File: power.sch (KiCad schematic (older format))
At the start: 38 parts, among them J2 USB_C_Receptacle_USB2.0, J3 TagConnect_TC2030_SWD, Q1 FS8205A, Q6 2N7002, Q7 AO3401A, SW8 SW_Push, U3 SY7088, U4 XC6206P332MR, U5 DW01+G, U6 TP4054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

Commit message: Add self-programming capability
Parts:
- removed C20, C21: 100nF, Capacitor_SMD:C_0402_1005Metric, symbol Device:C
- removed D5: PWR, Diode_SMD:D_0603_1608Metric, symbol Device:LED
- removed J3: TagConnect_TC2030_SWD, Connector:Tag-Connect_TC2030-IDC-NL_2x03_P1.27mm_Vertical, symbol Connector_TagConnect:TagConnect_TC2030_SWD
- removed R22: 8.2kR, Resistor_SMD:R_0402_1005Metric, symbol Device:R
- removed SW8: SW_Push, Button_Carbon:Button_Carbon_5mm, symbol Switch:SW_Push
- removed U8: STM32L011D3Px, Package_SO:TSSOP-14_4.4x5mm_P0.65mm, symbol MCU_ST_STM32L0:STM32L011D3Px
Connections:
- net labels removed: ~STMRST
- wire segments 156 -> 126
- no-connect marks 9 -> 3
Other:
- moved on the sheet: C11, C12, C13, C14, C15, C16, C17, C18, C19, D4, J2, L1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

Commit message: Add charge state/current sensing and VBUS wakeup source
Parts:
- added C?: 100nF, Capacitor_SMD:C_0402_1005Metric, symbol Device:C
- added F1, F2: Fuse, Fuse:Fuse_1206_3216Metric, symbol Device:Fuse
- added R? (x2): 8.2kR, Resistor_SMD:R_0402_1005Metric, symbol Device:R
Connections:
- net labels added: Ichg, LEDchg
- wire segments 126 -> 141
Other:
- moved on the sheet: TP1
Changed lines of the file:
@@
 L power:VBUS #PWR?
 U 1 1 6053CC12
-P 1700 3300
+P 1700 2950
 AR Path="/6053CC12" Ref="#PWR?"  Part="1"
 AR Path="/6051E9DC/6053CC12" Ref="#PWR023"  Part="1"
-F 0 "#PWR023" H 1700 3150 50  0001 C CNN
-F 1 "VBUS" H 1715 3473 50  0000 C CNN
-F 2 "" H 1700 3300 50  0001 C CNN
-F 3 "" H 1700 3300 50  0001 C CNN
-	1    1700 3300
+F 0 "#PWR023" H 1700 2800 50  0001 C CNN
+F 1 "VBUS" H 1715 3123 50  0000 C CNN
+F 2 "" H 1700 2950 50  0001 C CNN
+F 3 "" H 1700 2950 50  0001 C CNN
+	1    1700 2950
 	1    0    0    -1
 $EndComp
@@
 L Connector:TestPoint TP?
 U 1 1 6057E186
-P 4250 3550
+P 4250 3200
 AR Path="/6057E186" Ref="TP?"  Part="1"
 AR Path="/6051E9DC/6057E186" Ref="TP1"  Part="1"
-F 0 "TP1" H 4308 3668 50  0000 L CNN
-F 1 "BAT+" H 4308 3577 50  0000 L CNN
-F 2 "TestPoint:TestPoint_Pad_4.0x4.0mm" H 4450 3550 50  0001 C CNN
-F 3 "~" H 4450 3550 50  0001 C CNN
-	1    4250 3550
+F 0 "TP1" H 4308 3318 50  0000 L CNN
+F 1 "BAT+" H 4308 3227 50  0000 L CNN
+F 2 "TestPoint:TestPoint_Pad_4.0x4.0mm" H 4450 3200 50  0001 C CNN
+F 3 "~" H 4450 3200 50  0001 C CNN
+	1    4250 3200
 	1    0    0    -1
 $EndComp
@@
 	3700 3900 3650 3900
 Wire Wire Line
-	2700 3350 2700 3300
-Wire Wire Line
-	2700 4000 2700 4250
+	2700 4000 2700 4050
 $Comp
 L Device:LED D?
@@
 L power:VBUS #PWR?
 U 1 1 6057E1D9
-P 2700 3300
+P 2700 3250
 AR Path="/6057E1D9" Ref="#PWR?"  Part="1"
 AR Path="/6051E9DC/6057E1D9" Ref="#PWR037"  Part="1"
-F 0 "#PWR037" H 2700 3150 50  0001 C CNN
-F 1 "VBUS" H 2715 3473 50  0000 C CNN
-F 2 "" H 2700 3300 50  0001 C CNN
-F 3 "" H 2700 3300 50  0001 C CNN
-	1    2700 3300
+F 0 "#PWR037" H 2700 3100 50  0001 C CNN
+F 1 "VBUS" H 2715 3423 50  0000 C CNN
+F 2 "" H 2700 3250 50  0001 C CNN
+F 3 "" H 2700 3250 50  0001 C CNN
+	1    2700 3250
 	1    0    0    -1
 $EndComp
@@
 Text HLabel 9150 4850 0    50   Input ~ 0
 PWR_EN
+$Comp
+L Device:Fuse F1
+U 1 1 60F311E6
+P 1700 3150
+F 0 "F1" H 1760 3196 50  0000 L CNN
+F 1 "Fuse" H 1760 3105 50  0000 L CNN
+F 2 "Fuse:Fuse_1206_3216Metric" V 1630 3150 50  0001 C CNN
+F 3 "https://datasheet.lcsc.com/szlcsc/Shenzhen-lanson-Elec-12H1200C_C182310.pdf" H 1700 3150 50  0001 C CNN
+F 4 "C182310" H 1700 3150 50  0001 C CNN "LCSC"
+	1    1700 3150
+	1    0    0    -1
+$EndComp
+Wire Wire Line
+	1700 2950 1700 3000
+$Comp
+L Device:Fuse F2
+U 1 1 60F38C32
+P 4250 3400
+F 0 "F2" H 4310 3446 50  0000 L CNN
+F 1 "Fuse" H 4310 3355 50  0000 L CNN
+F 2 "Fuse:Fuse_1206_3216Metric" V 4180 3400 50  0001 C CNN
+F 3 "https://datasheet.lcsc.com/szlcsc/Shenzhen-lanson-Elec-12H1200C_C182310.pdf" H 4250 3400 50  0001 C CNN
+F 4 "C182310" H 4250 3400 50  0001 C CNN "LCSC"
+	1    4250 3400
+	-1   0    0    1
+$EndComp
+Wire Wire Line
+	4250 3250 4250 3200
+$Comp
+L Device:R R?
+U 1 1 60F9B087
+P 2500 4350
+AR Path="/60F9B087" Ref="R?"  Part="1"
+AR Path="/6051E9DC/60F9B087" Ref="R?"  Part="1"
+F 0 "R?" V 2293 4350 50  0000 C CNN
+F 1 "8.2kR" V 2384 4350 50  0000 C CNN
+F 2 "Resistor_SMD:R_0402_1005Metric" V 2430 4350 50  0001 C CNN
+F 3 "~" H 2500 4350 50  0001 C CNN
+F 4 "C25924" V 2500 4350 50  0001 C CNN "LCSC"
+	1    2500 4350
+	0    1    1    0
+$EndComp
+$Comp
+L Device:C C?
+U 1 1 60FA0E56
+P 2300 4550
+AR Path="/60FA0E56" Ref="C?"  Part="1"
+AR Path="/6051E9DC/60FA0E56" Ref="C?"  Part="1"
+F 0 "C?" V 2552 4550 50  0000 C CNN
+F 1 "100nF" V 2461 4550 50  0000 C CNN
+F 2 "Capacitor_SMD:C_0402_1005Metric" H 2338 4400 50  0001 C CNN
+F 3 "~" H 2300 4550 50  0001 C CNN
+F 4 "C1525" H 2300 4550 50  0001 C CNN "LCSC"
+	1    2300 4550
+	-1   0    0    1
+$EndComp
+Connection ~ 2700 4750
+Wire Wire Line
+	2650 4350 2700 4350
+Connection ~ 2700 4350
+Wire Wire Line
+	2300 4750 2300 4700
+Wire Wire Line
+	2300 4750 2700 4750
+Wire Wire Line
+	2350 4350 2300 4350
+Wire Wire Line
+	2300 4350 2300 4400
+Wire Wire Line
+	2250 4350 2300 4350
+Connection ~ 2300 4350
+Text HLabel 2250 4350 0    50   Output ~ 0
+Ichg
+$Comp
+L Device:R R?
+U 1 1 60FBF848
+P 2900 3500
+AR Path="/60FBF848" Ref="R?"  Part="1"
+AR Path="/6051E9DC/60FBF848" Ref="R?"  Part="1"
+F 0 "R?" V 2693 3500 50  0000 C CNN
+F 1 "8.2kR" V 2784 3500 50  0000 C CNN
+F 2 "Resistor_SMD:R_0402_1005Metric" V 2830 3500 50  0001 C CNN
+F 3 "~" H 2900 3500 50  0001 C CNN
+F 4 "C25924" V 2900 3500 50  0001 C CNN "LCSC"
+	1    2900 3500
+	-1   0    0    1
+$EndComp
+Wire Wire Line
+	2700 3250 2700 3300
+Wire Wire Line
+	2700 3300 2900 3300
+Wire Wire Line
+	2900 3300 2900 3350
+Connection ~ 2700 3300
+Wire Wire Line
+	2700 3300 2700 3350
+Wire Wire Line
+	2900 3650 2900 4050
+Wire Wire Line
+	2900 4050 2700 4050
+Connection ~ 2700 4050
+Wire Wire Line
+	2700 4050 2700 4250
+Text HLabel 2650 4050 0    50   Output ~ 0
+LEDchg
+Wire Wire Line
+	2650 4050 2700 4050
 $EndSCHEMATC

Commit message: Implement fuel gauging
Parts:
- added C27, C29: 100nF, Capacitor_SMD:C_0402_1005Metric, symbol Device:C
- added C28: 1uF, Capacitor_SMD:C_0402_1005Metric, symbol Device:C
- added R29: 1MR, Resistor_SMD:R_0402_1005Metric, symbol Device:R
- added R30, R31: 100R, Resistor_SMD:R_0402_1005Metric, symbol Device:R
- added R32: 25mR, Resistor_SMD:R_2512_6332Metric, symbol Device:R
- added TH1: 10kR 3380K, Resistor_SMD:R_0402_1005Metric, symbol Device:Thermistor_NTC
- added U9: BQ34Z100, Package_SO:TSSOP-14_4.4x5mm_P0.65mm, symbol Fuel_Gauge_TI:BQ34Z100
- gave numbers to parts that had none: 3
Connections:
- net labels added: GAUGE_EN, GNDREF, SCL, SDA, SHUNT+, SHUNT-
- wire segments 141 -> 183
- no-connect marks 3 -> 7

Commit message: Finish layout
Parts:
- removed U6: TP4054, Package_TO_SOT_SMD:TSOT-23-5, symbol Battery_Management:LTC4054ES5-4.2
- added C30: 100nF, Capacitor_SMD:C_0402_1005Metric, symbol Device:C
- added C31: 47uF, Capacitor_SMD:C_1206_3216Metric, symbol Device:C
- added Q8: 2N7002, Package_TO_SOT_SMD:SOT-23, symbol Transistor_FET:2N7002
- added R35: 1MR, Resistor_SMD:R_0402_1005Metric, symbol Device:R
- added R36: 8.2kR, Resistor_SMD:R_0402_1005Metric, symbol Device:R
- added U6: TP4056, Package_SO:HSOP-8-1EP_3.9x4.9mm_P1.27mm_EP2.41x3.1mm, symbol Battery_Management_Generic:TP4056
- C19: value 1uF -> 10uF; footprint Capacitor_SMD:C_0402_1005Metric -> Capacitor_SMD:C_0603_1608Metric; LCSC C52923 -> C19702
- C26: value 100nF -> 10uF; footprint Capacitor_SMD:C_0402_1005Metric -> Capacitor_SMD:C_0603_1608Metric; LCSC C1525 -> C19702
- R26: value 8.2kR -> 2.2kR; LCSC C25924 -> C25879
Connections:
- net labels added: ~PWR_EN
- wire segments 183 -> 205
- no-connect marks 7 -> 8
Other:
- note added: "Ichg=500mA/1A"
- note removed: "Ichg=450mA"
- moved on the sheet: C18, D4, F2, Q1, R12, R13, R14, R27, R32, TP1, TP2, U5

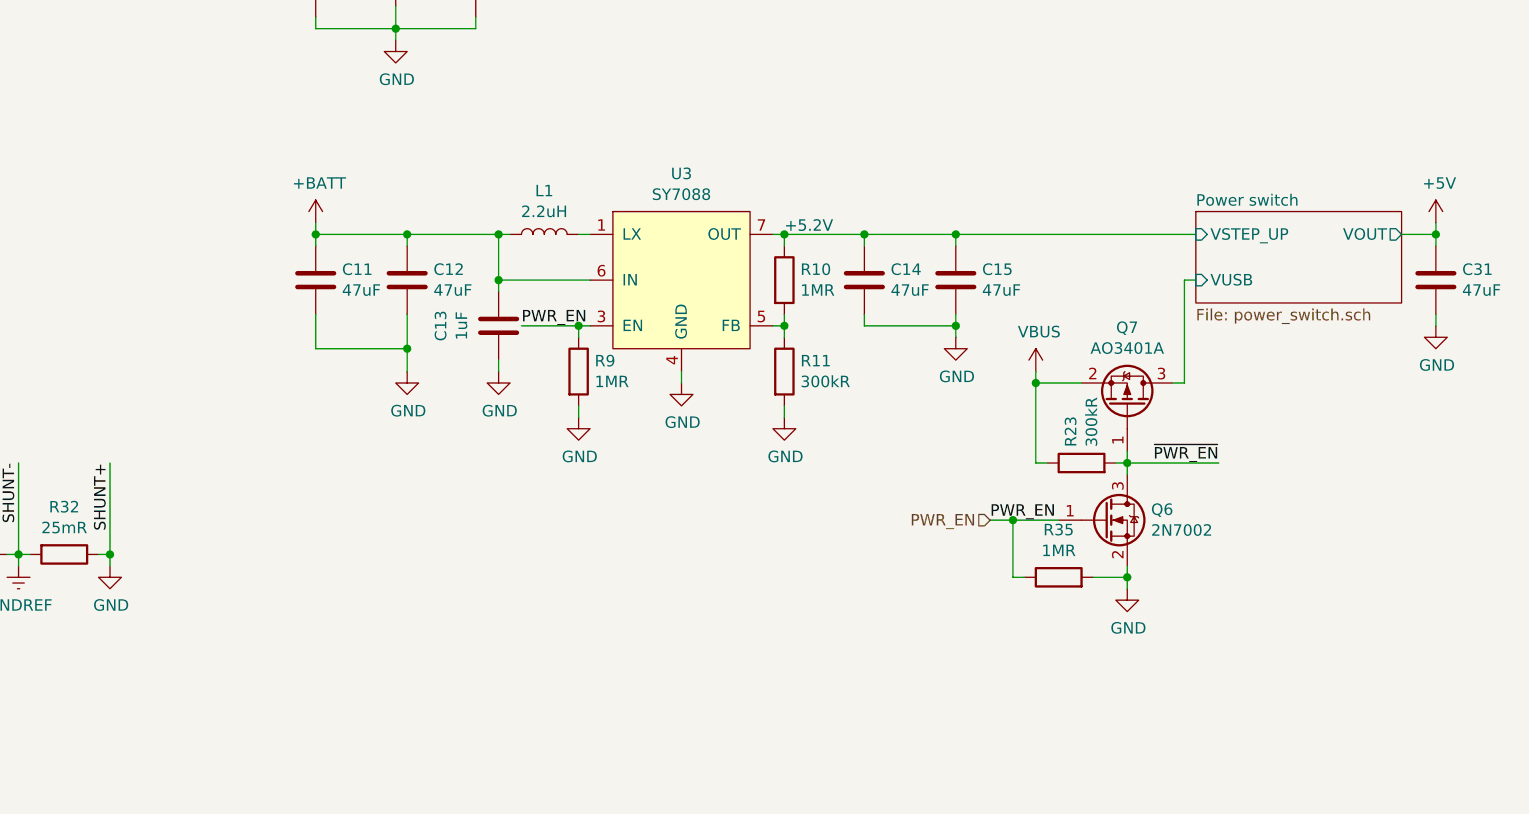
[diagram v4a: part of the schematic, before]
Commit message: Add additional mounting holes
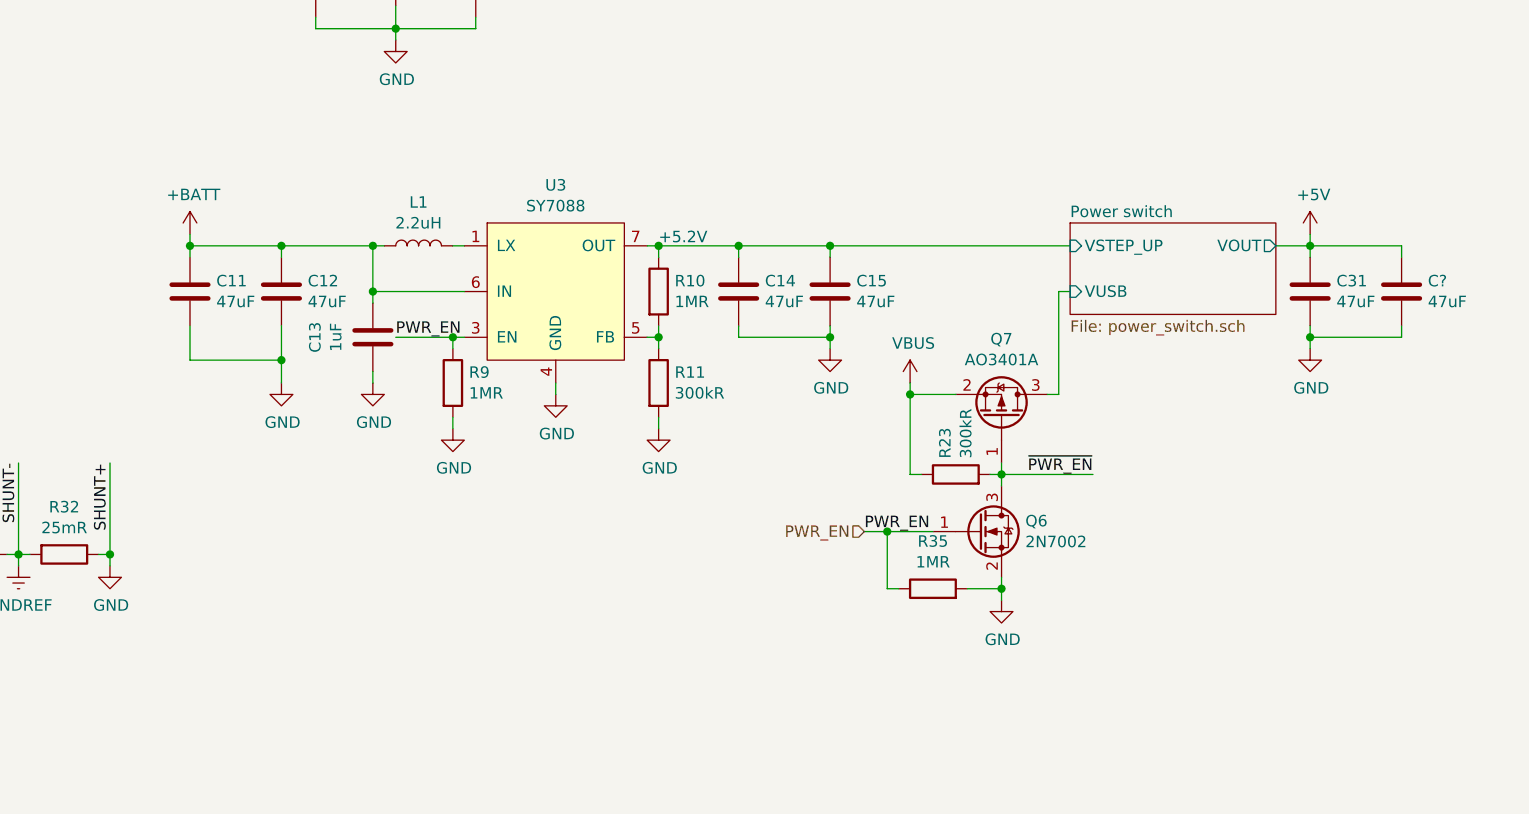
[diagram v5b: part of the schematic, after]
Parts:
- added C?: 47uF, Capacitor_SMD:C_1206_3216Metric, symbol Device:C
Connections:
- net +5V: now also C?.2
- net GND: now also C?.1
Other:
- moved on the sheet: C11, C12, C13, C14, C15, C31, L1, Q6, Q7, R10, R11, R23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

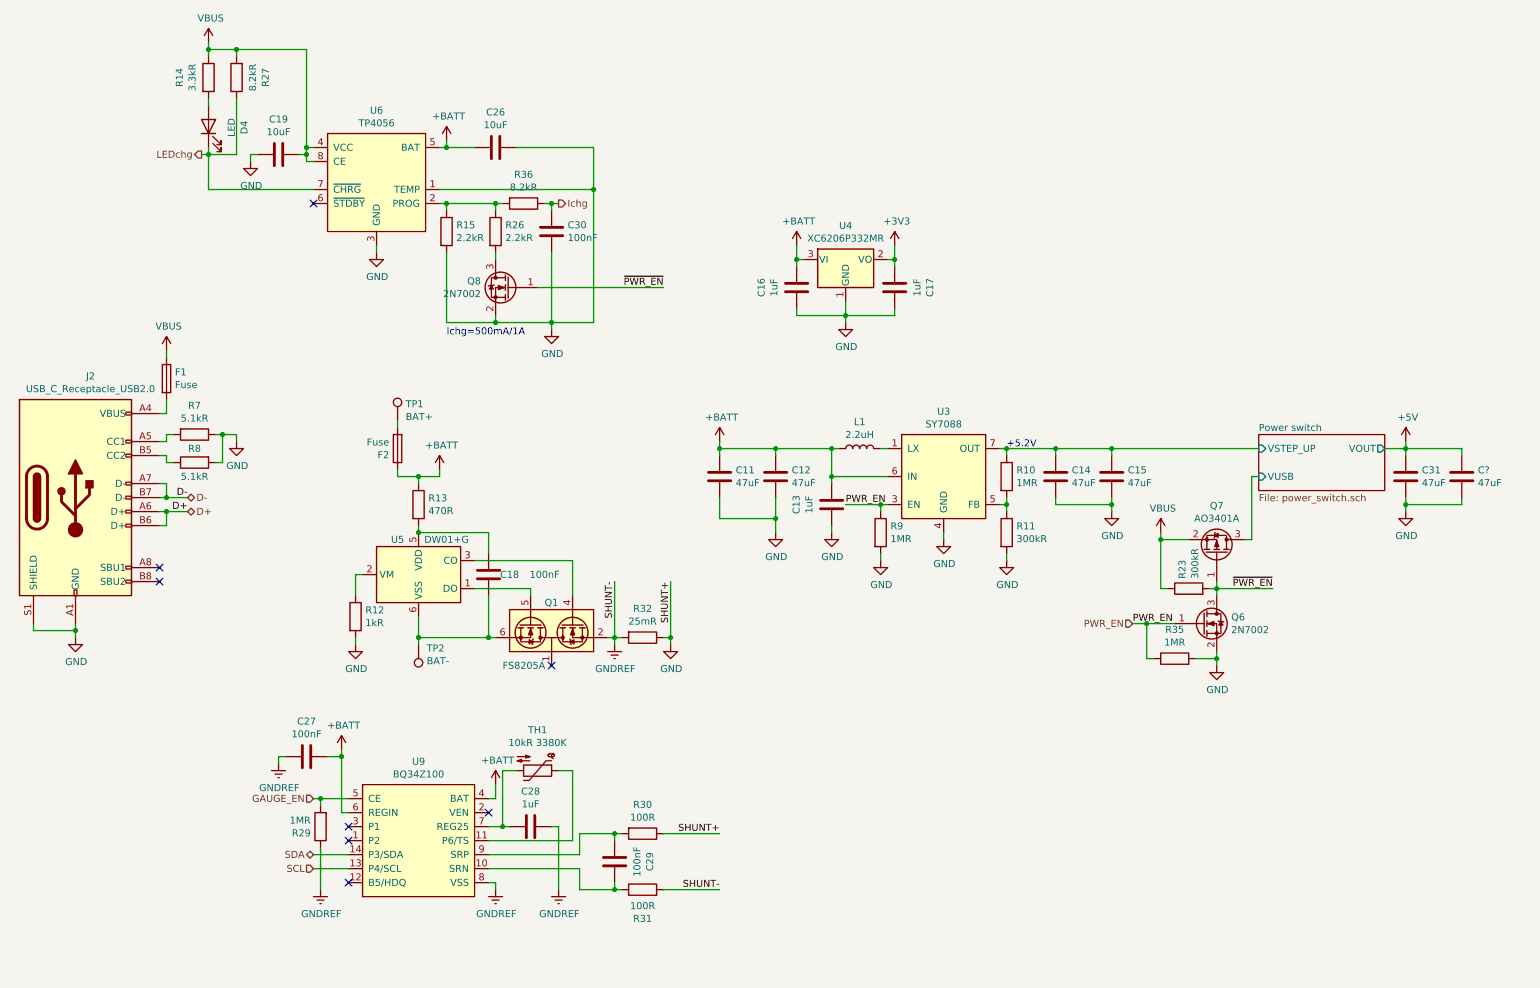
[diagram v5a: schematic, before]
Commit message: Replace test points by battery footprints
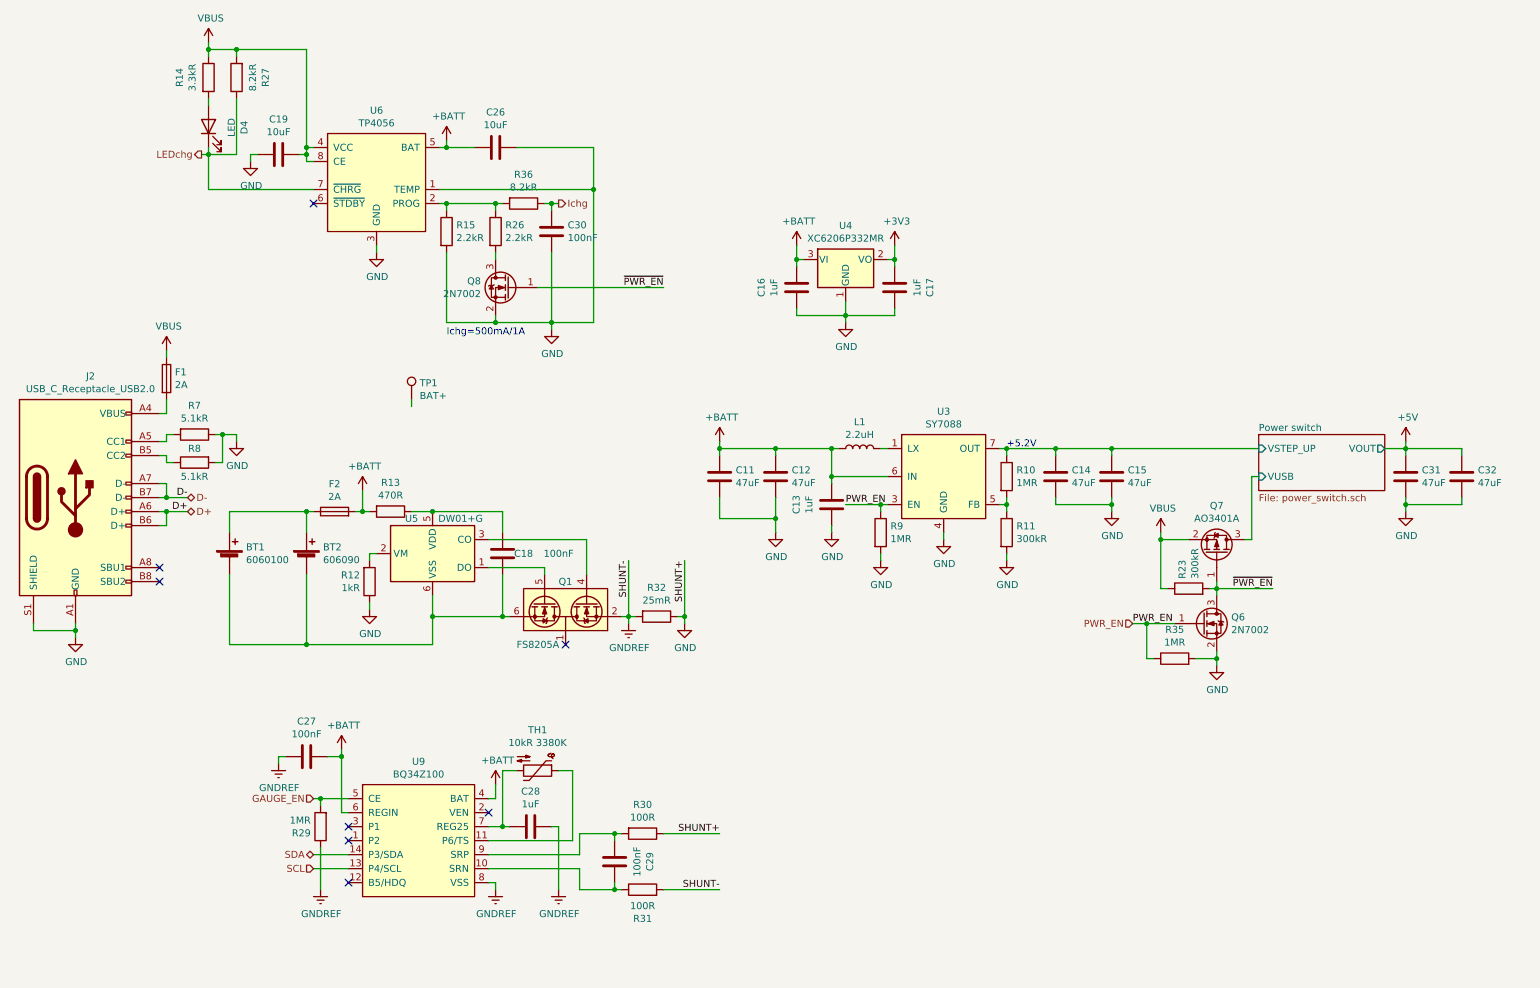
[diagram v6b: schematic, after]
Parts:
- removed TP2: BAT-, TestPoint:TestPoint_Pad_4.0x4.0mm, symbol Connector:TestPoint
- added BT1: 6060100, Battery_LiPo:LiPo_6060100, symbol Device:Battery_Cell
- added BT2: 606090, Battery_LiPo:LiPo_606090, symbol Device:Battery_Cell
- F1, F2: value Fuse -> 2A
- gave numbers to parts that had none: 1
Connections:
- net +BATT: now also F2.2, R13.2; no longer F2.1, R13.1
- net GND: now also R12.1; no longer R12.2
- net at U5.2 (VM): now also R12.2; no longer R12.1
- net at C18.2, U5.5 (VDD): now also R13.1; no longer R13.2
- net at C18.1, Q1.6, Q1.7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: now also BT1.2 (-), BT2.2 (-)
- net at TP1.1: no longer F2.2
- new net: BT1.1 (+), BT2.1 (+), F2.1
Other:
- moved on the sheet: C18, F2, Q1, R12, R13, R32, TP1, U5
